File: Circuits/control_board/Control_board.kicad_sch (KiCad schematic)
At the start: 10 parts

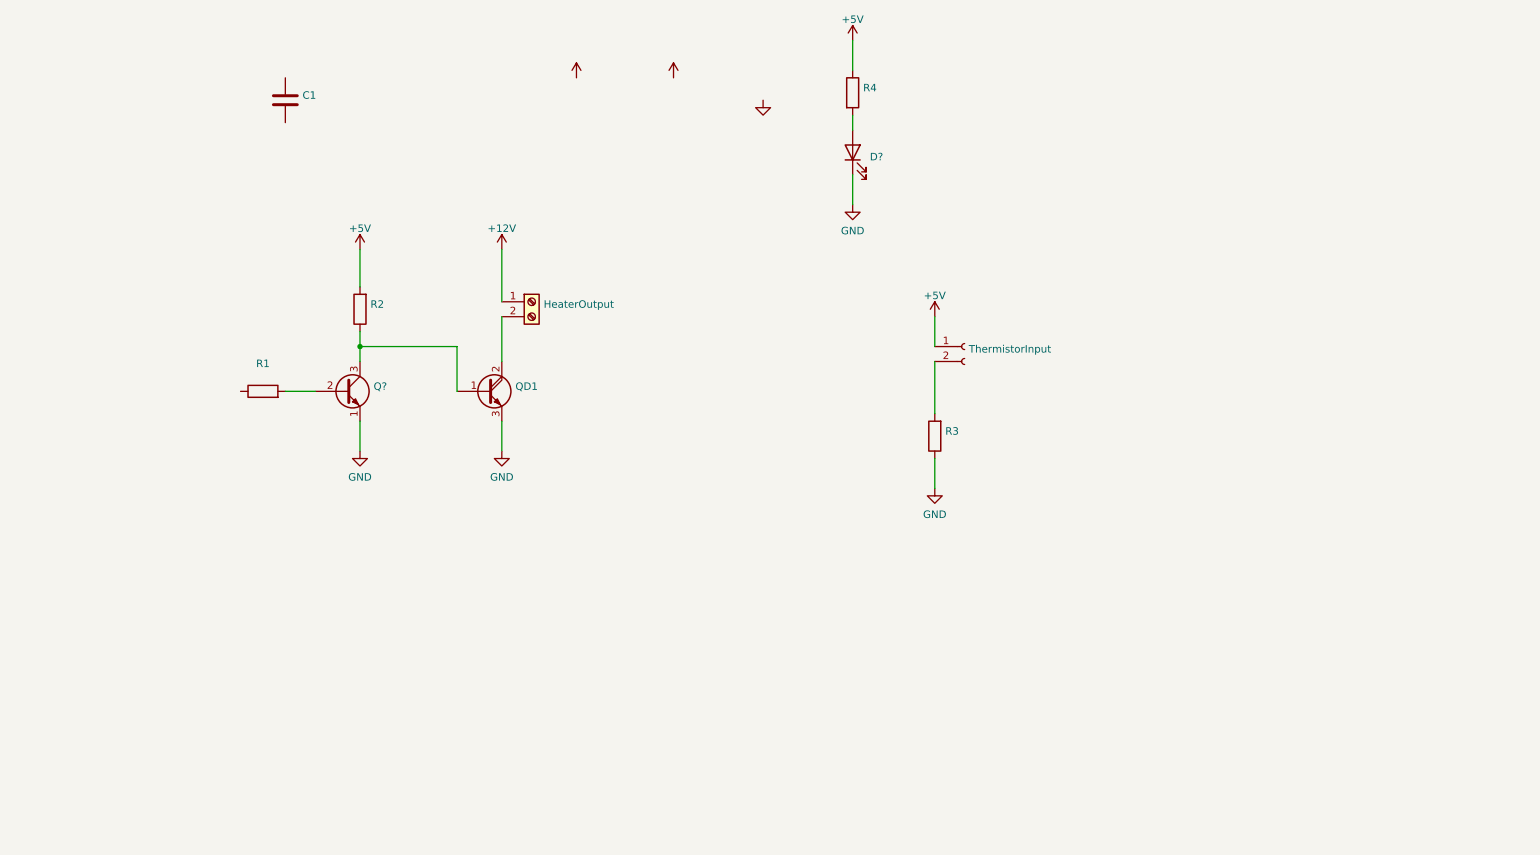
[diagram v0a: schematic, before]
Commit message: implemented PWM for npn circuit and added stirring circuit
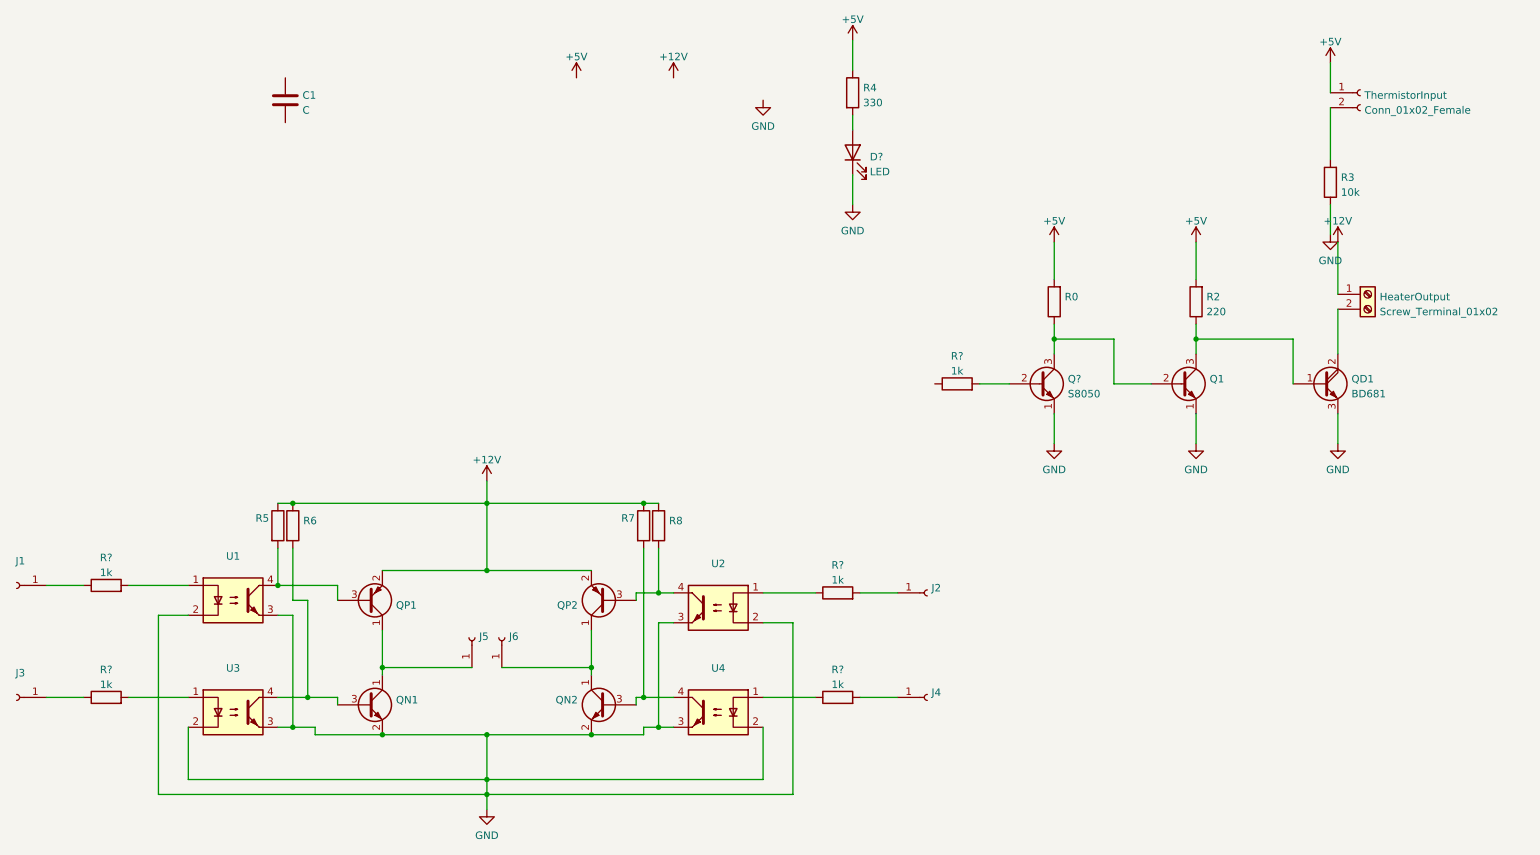
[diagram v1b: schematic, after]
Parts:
- removed R1: (no value), symbol Device:R
- added J1, J2, J3, J4, J5, J6: (no value), symbol Connector:Conn_01x01_Female
- added Q?: S8050, Package_TO_SOT_THT:TO-92_Inline, symbol Transistor_BJT:S8050
- added QN1, QN2: (no value), symbol Device:Q_NPN_CEB
- added QP1, QP2: (no value), symbol Device:Q_PNP_CEB
- added R0, R5, R6, R7, R8: (no value), symbol Device:R
- added R? (x5): 1k, Resistor_THT:R_Axial_DIN0207_L6.3mm_D2.5mm_P7.62mm_Horizontal, symbol Device:R
- added U1, U2, U3, U4: (no value), symbol Isolator:PC817
- C1: value (none) -> C; footprint (none) -> Capacitor_THT:C_Disc_D5.0mm_W2.5mm_P2.50mm
- D?: value (none) -> LED
- HeaterOutput: value (none) -> Screw_Terminal_01x02; footprint (none) -> TerminalBlock:TerminalBlock_bornier-2_P5.08mm
- QD1: value (none) -> BD681; footprint (none) -> Package_TO_SOT_THT:TO-126-3_Vertical
- R2: value (none) -> 220; footprint (none) -> Resistor_THT:R_Axial_DIN0207_L6.3mm_D2.5mm_P7.62mm_Horizontal
- R3: value (none) -> 10k; footprint (none) -> Resistor_THT:R_Axial_DIN0207_L6.3mm_D2.5mm_P7.62mm_Horizontal
- R4: value (none) -> 330; footprint (none) -> Resistor_THT:R_Axial_DIN0207_L6.3mm_D2.5mm_P7.62mm_Horizontal
- ThermistorInput: value (none) -> Conn_01x02_Female; footprint (none) -> Connector_JST:JST_EH_B2B-EH-A_1x02_P2.50mm_Vertical
- gave numbers to parts that had none: 1
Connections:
- net +12V: now also QP1.2 (E), QP2.2 (E), R5.1, R6.1, R7.1, R8.1
- net +5V: now also R0.2
- net GND: now also Q?.1 (E), QN1.2 (E), QN2.2 (E), U1.2, U1.3, U2.2, U2.3, U3.2, U3.3, U4.2, U4.3
- net at Q1.2 (B): now also Q?.3 (C), R0.1
- new net: R?.2, U3.1
- new net: QN1.3 (B), R6.2, U3.4
- new net: J3.1 (Pin_1), R?.1
- new net: J6.1 (Pin_1), QN2.1 (C), QP2.1 (C)
- new net: QP2.3 (B), R8.2, U2.4
- new net: R?.1, U4.1
- new net: J4.1 (Pin_1), R?.2
- new net: Q?.2 (B), R?.2
- new net: QN2.3 (B), R7.2, U4.4
- new net: J5.1 (Pin_1), QN1.1 (C), QP1.1 (C)
- new net: QP1.3 (B), R5.2, U1.4
- new net: R?.1, U2.1
- new net: J1.1 (Pin_1), R?.1
- new net: R?.2, U1.1
- new net: J2.1 (Pin_1), R?.2
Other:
- moved on the sheet: HeaterOutput, Q1, QD1, R2, R3, ThermistorInput
